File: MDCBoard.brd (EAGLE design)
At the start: 43.9 x 32.6 mm, 200 parts, among them J1 JUMPER-SOLDER, J10 MICROSD-SOCKET, J11 USB-C-RECEPTACLE-KOREANHRO, J2 JUMPER-SOLDER, J3 JUMPER-SOLDER, J4 JUMPER-SOLDER, J5 JST-SM02B-SRSS-TB, J6 JUMPER-SOLDER, J7 JUMPER-SOLDER, J8 JUMPER-SOLDER, Q1 PMOS-NEXPERIA-SOT1220, Q2 PMOS-NEXPERIA-SOT1220, Q3 PMOS-NEXPERIA-SOT1220, Q4 DIODESINC-DMG2305UX, Q5 DIODESINC-DMG2305UX, Q6 DIODESINC-DMG2305UX, Q7 DIODESINC-DMG2305UX, Q8 DIODESINC-DMG2305UX, U1 TI-TPS2116, U10 TI-TPS22919DCK, U11 TI-TPS22919DCK, U12 TI-TPS22919DCK, U13 TI-TPS22919DCK, U14 TI-MSP430FR2422IRHL, U16 TI-TXB0102, U17 PANASONIC-EKMB110711X, U18 LATTICE-ICE40HX4K-BG121, U19 WINBOND-W25Q40EW, U2 DIODESINC-AP7350, U20 NEXPERIA-74LVC1G98-OR-INV-INP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, U21 NEXPERIA-74LVC1G98-BUFFER, U22 ON-AR0330CS1C12SPKA0, U23 ALLIANCE-AS4C8M16MSA-6BIN, U24 STM-STM32F730, U25 DIODESINC-DT1446-04V-7, U26 NEXPERIA-74LVC1G98-INVERTER, U3 NEXPERIA-74LVC1G98-NOR, U4 MICROCHIP-MCP7383X, U5 NEXPERIA-74LVC1G98-INVERTER, U6 EATON-STN101, U7 TI-TPS62A01, U8 TI-TPS62A01, U9 TI-TPS62A01, X1 EPSON-FC-135, X2 SITIME-SIT8021, X3 SITIME-SIT8021

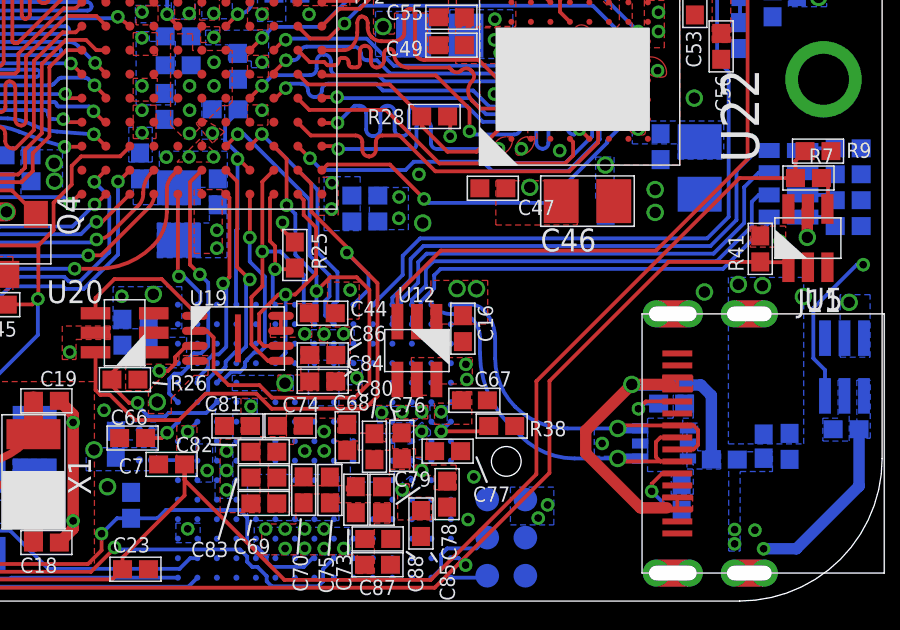
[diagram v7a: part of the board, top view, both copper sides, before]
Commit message: 12 airwires
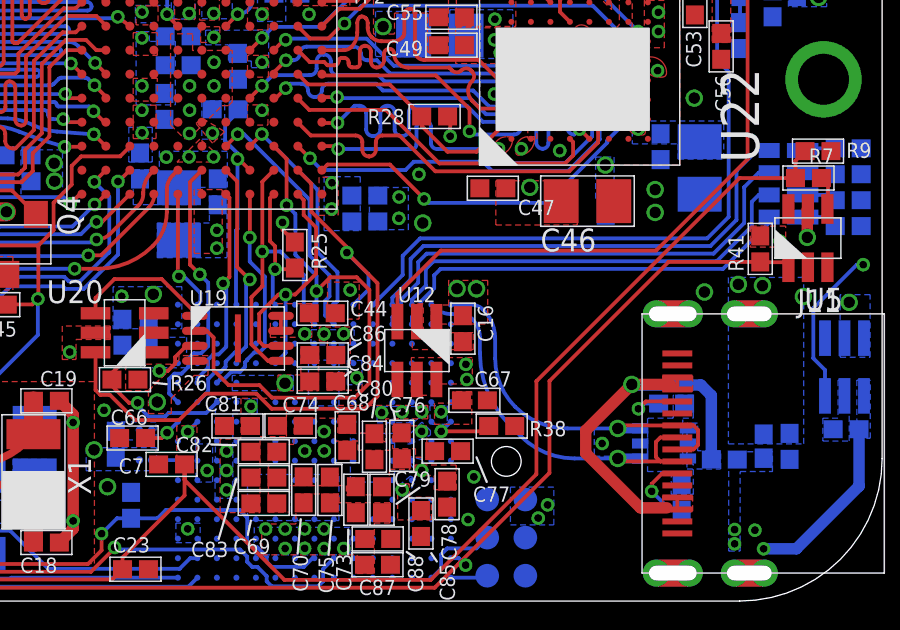
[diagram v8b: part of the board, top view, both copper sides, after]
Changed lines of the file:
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@@
 <grid distance="10" unitdist="mil" unit="mil" style="lines" multiple="1" display="no" altdistance="0.00254" altunitdist="mm" altunit="mil"/>
 <layers>
-<layer number="1" name="Top" color="4" fill="1" visible="no" active="yes"/>
+<layer number="1" name="Top" color="4" fill="1" visible="yes" active="yes"/>
 <layer number="2" name="Ground" color="16" fill="1" visible="no" active="yes"/>
 <layer number="3" name="Route3" color="17" fill="1" visible="no" active="no"/>
@@
 <layer number="14" name="Route14" color="22" fill="1" visible="no" active="no"/>
 <layer number="15" name="Power" color="42" fill="1" visible="no" active="yes"/>
-<layer number="16" name="Bottom" color="1" fill="1" visible="yes" active="yes"/>
+<layer number="16" name="Bottom" color="1" fill="1" visible="no" active="yes"/>
 <layer number="17" name="Pads" color="2" fill="1" visible="yes" active="yes"/>
 <layer number="18" name="Vias" color="2" fill="1" visible="yes" active="yes"/>
 <layer number="19" name="Unrouted" color="6" fill="1" visible="no" active="yes"/>
 <layer number="20" name="Dimension" color="24" fill="1" visible="yes" active="yes"/>
-<layer number="21" name="tPlace" color="7" fill="1" visible="no" active="yes"/>
-<layer number="22" name="bPlace" color="7" fill="1" visible="yes" active="yes"/>
-<layer number="23" name="tOrigins" color="15" fill="1" visible="no" active="yes"/>
-<layer number="24" name="bOrigins" color="15" fill="1" visible="yes" active="yes"/>
-<layer number="25" name="tNames" color="7" fill="1" visible="no" active="yes"/>
-<layer number="26" name="bNames" color="7" fill="1" visible="yes" active="yes"/>
-<layer number="27" name="tValues" color="7" fill="1" visible="no" active="yes"/>
-<layer number="28" name="bValues" color="7" fill="1" visible="yes" active="yes"/>
-<layer number="29" name="tStop" color="7" fill="3" visible="no" active="yes"/>
-<layer number="30" name="bStop" color="7" fill="6" visible="yes" active="yes"/>
-<layer number="31" name="tCream" color="7" fill="4" visible="no" active="yes"/>
-<layer number="32" name="bCream" color="7" fill="5" visible="yes" active="yes"/>
-<layer number="33" name="tFinish" color="6" fill="3" visible="no" active="yes"/>
-<layer number="34" name="bFinish" color="6" fill="6" visible="yes" active="yes"/>
-<layer number="35" name="tGlue" color="7" fill="4" visible="no" active="yes"/>
-<layer number="36" name="bGlue" color="7" fill="5" visible="yes" active="yes"/>
-<layer number="37" name="tTest" color="7" fill="1" visible="no" active="yes"/>
-<layer number="38" name="bTest" color="7" fill="1" visible="yes" active="yes"/>
-<layer number="39" name="tKeepout" color="4" fill="11" visible="no" active="yes"/>
-<layer number="40" name="bKeepout" color="1" fill="11" visible="yes" active="yes"/>
-<layer number="41" name="tRestrict" color="4" fill="10" visible="no" active="yes"/>
-<layer number="42" name="bRestrict" color="1" fill="10" visible="yes" active="yes"/>
+<layer number="21" name="tPlace" color="7" fill="1" visible="yes" active="yes"/>
+<layer number="22" name="bPlace" color="7" fill="1" visible="no" active="yes"/>
+<layer number="23" name="tOrigins" color="15" fill="1" visible="yes" active="yes"/>
+<layer number="24" name="bOrigins" color="15" fill="1" visible="no" active="yes"/>
+<layer number="25" name="tNames" color="7" fill="1" visible="yes" active="yes"/>
+<layer number="26" name="bNames" color="7" fill="1" visible="no" active="yes"/>
+<layer number="27" name="tValues" color="7" fill="1" visible="yes" active="yes"/>
+<layer number="28" name="bValues" color="7" fill="1" visible="no" active="yes"/>
+<layer number="29" name="tStop" color="7" fill="3" visible="yes" active="yes"/>
+<layer number="30" name="bStop" color="7" fill="6" visible="no" active="yes"/>
+<layer number="31" name="tCream" color="7" fill="4" visible="yes" active="yes"/>
+<layer number="32" name="bCream" color="7" fill="5" visible="no" active="yes"/>
+<layer number="33" name="tFinish" color="6" fill="3" visible="yes" active="yes"/>
+<layer number="34" name="bFinish" color="6" fill="6" visible="no" active="yes"/>
+<layer number="35" name="tGlue" color="7" fill="4" visible="yes" active="yes"/>
+<layer number="36" name="bGlue" color="7" fill="5" visible="no" active="yes"/>
+<layer number="37" name="tTest" color="7" fill="1" visible="yes" active="yes"/>
+<layer number="38" name="bTest" color="7" fill="1" visible="no" active="yes"/>
+<layer number="39" name="tKeepout" color="4" fill="11" visible="yes" active="yes"/>
+<layer number="40" name="bKeepout" color="1" fill="11" visible="no" active="yes"/>
+<layer number="41" name="tRestrict" color="4" fill="10" visible="yes" active="yes"/>
+<layer number="42" name="bRestrict" color="1" fill="10" visible="no" active="yes"/>
 <layer number="43" name="vRestrict" color="2" fill="10" visible="no" active="yes"/>
 <layer number="44" name="Drills" color="7" fill="1" visible="no" active="yes"/>
@@
 </polygon>
 <polygon width="0.127" layer="1" thermals="no">
-<vertex x="28.81478125" y="10.68831875"/>
-<vertex x="28.81478125" y="8.7757"/>
-<vertex x="29.178" y="8.7757"/>
-<vertex x="29.178" y="9.2329"/>
+<vertex x="30.70708125" y="10.68831875"/>
+<vertex x="29.405578125" y="10.68831875"/>
+<vertex x="29.405578125" y="9.8679"/>
+<vertex x="28.8264625" y="9.8679"/>
+<vertex x="28.8264625" y="9.2329"/>
 <vertex x="30.70708125" y="9.2329"/>
-<vertex x="30.70708125" y="10.68831875"/>
 </polygon>
 <via x="24.125940625" y="22.4180375" extent="1-16" drill="0.381"/>
@@
 <via x="38.707059375" y="26.007059375" extent="1-16" drill="0.381"/>
 <via x="28.374340625" y="30.1777375" extent="1-16" drill="0.254"/>
+<polygon width="0.127" layer="1" thermals="no" rank="2">
+<vertex x="28.194" y="9.906"/>
+<vertex x="28.194" y="8.382"/>
+<vertex x="30.226" y="8.382"/>
+<vertex x="30.226" y="8.945878125"/>
+<vertex x="28.559759375" y="8.945878125"/>
+<vertex x="28.559759375" y="9.906"/>
+</polygon>
 <wire x1="27.192578125" y1="24.960959375" x2="27.0676375" y2="26.110340625" width="0" layer="19" extent="1-16"/>
 <wire x1="29.2735" y1="28.2537375" x2="28.916" y2="29.437740625" width="0" layer="19" extent="1-16"/>
 <wire x1="21.93470625" y1="5.83590625" x2="21.030403125" y2="4.67901875" width="0" layer="19" extent="1-16"/>
 <wire x1="30.695915625" y1="6.69100625" x2="29.8034625" y2="4.99618125" width="0" layer="19" extent="1-1"/>
-<wire x1="28.346978125" y1="9.3113625" x2="29.8810375" y2="8.646903125" width="0" layer="19" extent="1-1"/>
 <wire x1="19.398978125" y1="1.0617125" x2="18.8195125" y2="3.623815625" width="0" layer="19" extent="1-16"/>
 </signal>
